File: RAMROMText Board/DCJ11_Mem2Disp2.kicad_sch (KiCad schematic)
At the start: 33 parts, among them J1 86093967113745ELF, U1 HM62256BLP, U2 SST39SF010, U3 GAL16V8, U4 74AHC138, U5 HM62256BLP, U6 SST39SF010

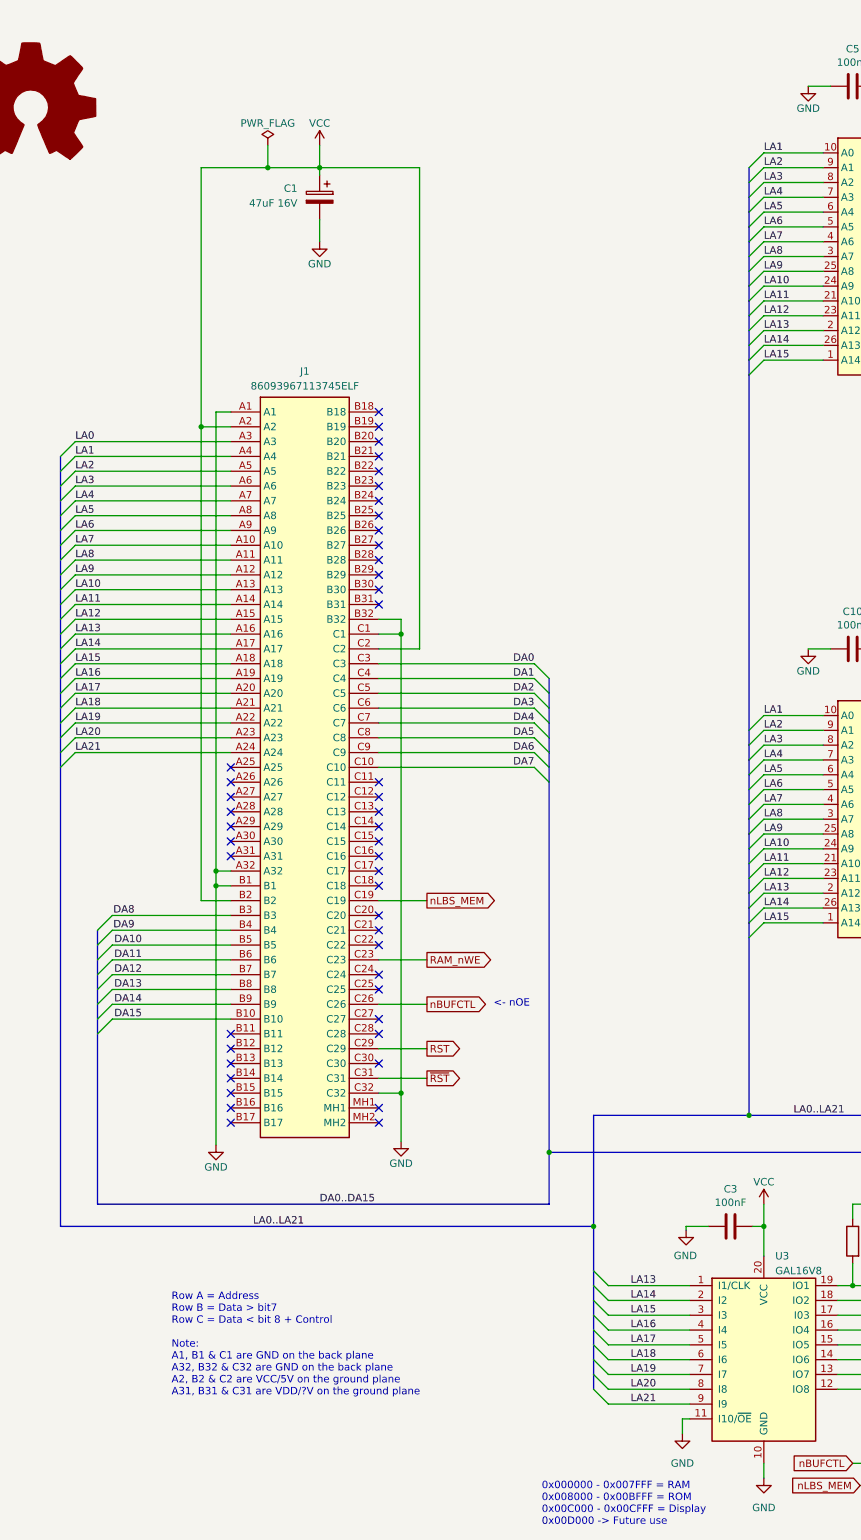
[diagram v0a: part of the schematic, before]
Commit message: Adjust memory map
Moved the memory map around so that I can add the dotmatrix display I want to add. These are now;

HEX
0x0000 - 0x7FFF = RAM  (32K)
0x6000 - 0x7FFF = Text Display (shadowed in RAM as it's WRITE only)
0x8000 - 0xBFFF = ROM  (16K)
0xC000 - 0xDFFF = Future (Matrix display)
0xE000 - 0xFFFF = Future

OCTAL (has to end on a multiple of 2)
000 000 - 077 776 - RAM
060 000 - 060 020 - Text Display (repeated multiple times)
100 000 - 137 776 - ROM
140 000 - 157 776 - Future (Matrix Display)
160 000 - 177 776 - Future
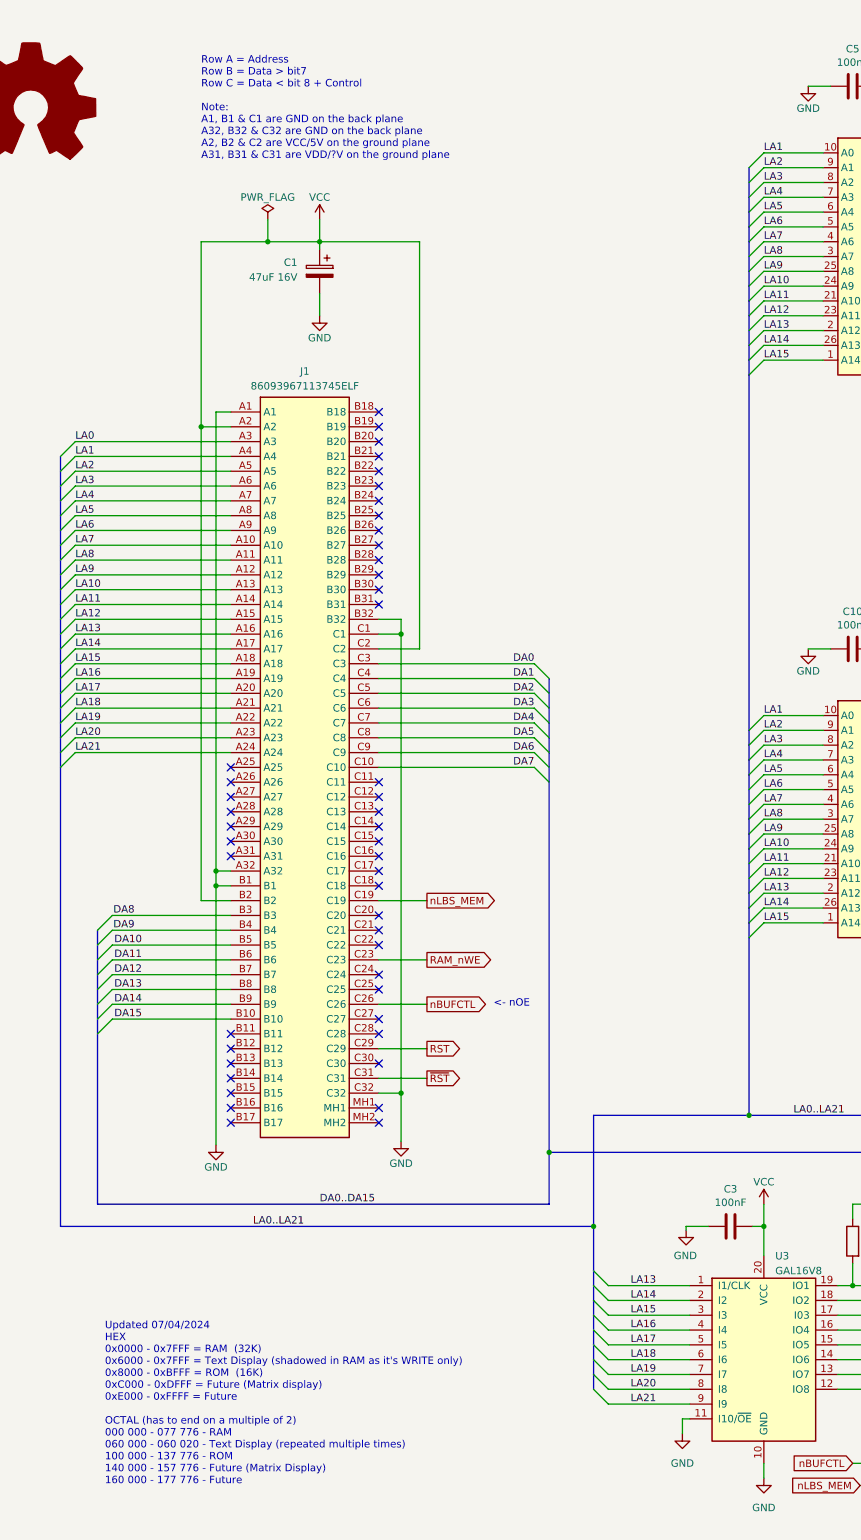
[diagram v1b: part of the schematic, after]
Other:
- note added: "Updated 07/04/2024 HEX 0x0000 - 0x7FFF = RAM (32K) 0x6000 - 0x7FFF = Text Display (shadowed in RAM as it's WRITE only) 0x8000 - 0xBFFF = ROM (16K) 0xC000 - 0xDFFF = Future (Matrix display) 0xE000 - 0xFFFF = Future OCTAL (has to end on a multiple of 2) 000 000 - 077 776 - RAM 060 000 - 060 020 - Text Display (repeated multiple times) 100 000 - 137 776 - ROM 140 000 - 157 776 - Future (Matrix Displ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"
- note removed: "0x000000 - 0x007FFF = RAM 0x008000 - 0x00BFFF = ROM 0x00C000 - 0x00CFFF = Display 0x00D000 -> Future use"
- moved on the sheet: C1
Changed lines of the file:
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@@
   (junction (at 347.98 105.41) (diameter 0) (color 0 0 0 0)
   )
-  (junction (at 81.28 45.72) (diameter 0) (color 0 0 0 0)
+  (junction (at 81.28 58.42) (diameter 0) (color 0 0 0 0)
   )
   (junction (at 154.94 208.28) (diameter 0) (color 0 0 0 0)
   )
-  (junction (at 72.39 45.72) (diameter 0) (color 0 0 0 0)
+  (junction (at 72.39 58.42) (diameter 0) (color 0 0 0 0)
   )
   (junction (at 336.55 48.26) (diameter 0) (color 0 0 0 0)
@@
     (stroke (width 0) (type default))
   )
-  (wire (pts (xy 98.425 45.72) (xy 98.425 128.27))
+  (wire (pts (xy 98.425 58.42) (xy 98.425 128.27))
     (stroke (width 0) (type default))
   )
@@
     (stroke (width 0) (type default))
   )
-  (wire (pts (xy 81.28 45.72) (xy 72.39 45.72))
+  (wire (pts (xy 81.28 58.42) (xy 72.39 58.42))
     (stroke (width 0) (type default))
   )
@@
     (stroke (width 0) (type default))
   )
-  (wire (pts (xy 72.39 45.72) (xy 72.39 41.91))
+  (wire (pts (xy 72.39 58.42) (xy 72.39 54.61))
     (stroke (width 0) (type default))
   )
@@
     (stroke (width 0) (type default))
   )
-  (wire (pts (xy 60.96 45.72) (xy 72.39 45.72))
+  (wire (pts (xy 60.96 58.42) (xy 72.39 58.42))
     (stroke (width 0) (type default))
   )
@@
     (stroke (width 0) (type default))
   )
-  (wire (pts (xy 81.28 45.72) (xy 81.28 41.91))
+  (wire (pts (xy 81.28 58.42) (xy 81.28 54.61))
     (stroke (width 0) (type default))
   )
@@
     (stroke (width 0) (type default))
   )
-  (wire (pts (xy 60.96 90.17) (xy 60.96 45.72))
+  (wire (pts (xy 60.96 90.17) (xy 60.96 58.42))
     (stroke (width 0) (type default))
   )
@@
     (stroke (width 0) (type default))
   )
-  (wire (pts (xy 81.28 54.61) (xy 81.28 58.42))
+  (wire (pts (xy 81.28 67.31) (xy 81.28 71.12))
     (stroke (width 0) (type default))
   )
@@
     (stroke (width 0) (type default))
   )
-  (wire (pts (xy 81.28 45.72) (xy 81.28 46.99))
+  (wire (pts (xy 81.28 58.42) (xy 81.28 59.69))
     (stroke (width 0) (type default))
   )
@@
     (stroke (width 0) (type default))
   )
-  (wire (pts (xy 81.28 45.72) (xy 98.425 45.72))
+  (wire (pts (xy 81.28 58.42) (xy 98.425 58.42))
     (stroke (width 0) (type default))
   )
@@
     (stroke (width 0) (type default))
   )
-  (text "0x000000 - 0x007FFF = RAM\n0x008000 - 0x00BFFF = ROM\n0x00C000 - 0x00CFFF = Display\n0x00D000 -> Future use\n"
-    (at 119.38 278.765 0)
+  (text "Updated 07/04/2024\nHEX\n0x0000 - 0x7FFF = RAM  (32K)\n0x6000 - 0x7FFF = Text Display (shadowed in RAM as it's WRITE only)\n0x8000 - 0xBFFF = ROM  (16K)\n0xC000 - 0xDFFF = Future (Matrix display)\n0xE000 - 0xFFFF = Future\n\nOCTAL (has to end on a multiple of 2)\n000 000 - 077 776 - RAM\n060 000 - 060 020 - Text Display (repeated multiple times)\n100 000 - 137 776 - ROM\n140 000 - 157 776 - Future (Matrix Display)\n160 000 - 177 776 - Future"
+    (at 44.45 271.78 0)
     (effects (font (size 1.27 1.27)) (justify left bottom))
   )
@@
   )
   (text "Row A = Address\nRow B = Data > bit7\nRow C = Data < bit 8 + Control\n\nNote:\nA1, B1 & C1 are GND on the back plane\nA32, B32 & C32 are GND on the back plane\nA2, B2 & C2 are VCC/5V on the ground plane\nA31, B31 & C31 are VDD/?V on the ground plane"
-    (at 55.88 256.54 0)
+    (at 60.96 44.45 0)
     (effects (font (size 1.27 1.27)) (justify left bottom))
   )
@@
     )
   )
-  (symbol (lib_id "power:PWR_FLAG") (at 72.39 41.91 0) (mirror y) (unit 1)
+  (symbol (lib_id "power:PWR_FLAG") (at 72.39 54.61 0) (mirror y) (unit 1)
     (in_bom yes) (on_board yes) (dnp no) (fields_autoplaced)
-    (property "Reference" "#FLG01" (at 72.39 40.005 0)
+    (property "Reference" "#FLG01" (at 72.39 52.705 0)
       (effects (font (size 1.27 1.27)) hide)
     )
-    (property "Value" "PWR_FLAG" (at 72.39 38.1 0)
+    (property "Value" "PWR_FLAG" (at 72.39 50.8 0)
       (effects (font (size 1.27 1.27)))
     )
-    (property "Footprint" "" (at 72.39 41.91 0)
+    (property "Footprint" "" (at 72.39 54.61 0)
       (effects (font (size 1.27 1.27)) hide)
     )
-    (property "Datasheet" "~" (at 72.39 41.91 0)
+    (property "Datasheet" "~" (at 72.39 54.61 0)
       (effects (font (size 1.27 1.27)) hide)
     )
@@
     )
   )
-  (symbol (lib_id "power:VCC") (at 81.28 41.91 0) (mirror y) (unit 1)
+  (symbol (lib_id "power:VCC") (at 81.28 54.61 0) (mirror y) (unit 1)
     (in_bom yes) (on_board yes) (dnp no) (fields_autoplaced)
-    (property "Reference" "#PWR02" (at 81.28 45.72 0)
+    (property "Reference" "#PWR02" (at 81.28 58.42 0)
       (effects (font (size 1.27 1.27)) hide)
     )
-    (property "Value" "VCC" (at 81.28 38.1 0)
+    (property "Value" "VCC" (at 81.28 50.8 0)
       (effects (font (size 1.27 1.27)))
     )
-    (property "Footprint" "" (at 81.28 41.91 0)
+    (property "Footprint" "" (at 81.28 54.61 0)
       (effects (font (size 1.27 1.27)) hide)
     )
-    (property "Datasheet" "" (at 81.28 41.91 0)
+    (property "Datasheet" "" (at 81.28 54.61 0)
       (effects (font (size 1.27 1.27)) hide)
     )
@@
     )
   )
-  (symbol (lib_id "power:GND") (at 81.28 58.42 0) (mirror y) (unit 1)
+  (symbol (lib_id "power:GND") (at 81.28 71.12 0) (mirror y) (unit 1)
     (in_bom yes) (on_board yes) (dnp no)
-    (property "Reference" "#PWR03" (at 81.28 64.77 0)
+    (property "Reference" "#PWR03" (at 81.28 77.47 0)
       (effects (font (size 1.27 1.27)) hide)
     )
-    (property "Value" "GND" (at 81.28 62.23 0)
+    (property "Value" "GND" (at 81.28 74.93 0)
       (effects (font (size 1.27 1.27)))
     )
-    (property "Footprint" "" (at 81.28 58.42 0)
+    (property "Footprint" "" (at 81.28 71.12 0)
       (effects (font (size 1.27 1.27)) hide)
     )
-    (property "Datasheet" "" (at 81.28 58.42 0)
+    (property "Datasheet" "" (at 81.28 71.12 0)
       (effects (font (size 1.27 1.27)) hide)
     )
@@
     )
   )
-  (symbol (lib_id "Device:C_Polarized") (at 81.28 50.8 0) (mirror y) (unit 1)
+  (symbol (lib_id "Device:C_Polarized") (at 81.28 63.5 0) (mirror y) (unit 1)
     (in_bom yes) (on_board yes) (dnp no) (fields_autoplaced)
-    (property "Reference" "C1" (at 77.47 49.276 0)
+    (property "Reference" "C1" (at 77.47 61.976 0)
       (effects (font (size 1.27 1.27)) (justify left))
     )
-    (property "Value" "47uF 16V" (at 77.47 51.816 0)
+    (property "Value" "47uF 16V" (at 77.47 64.516 0)
       (effects (font (size 1.27 1.27)) (justify left))
     )
-    (property "Footprint" "Capacitor_SMD:CP_Elec_6.3x5.8" (at 80.3148 54.61 0)
+    (property "Footprint" "Capacitor_SMD:CP_Elec_6.3x5.8" (at 80.3148 67.31 0)
       (effects (font (size 1.27 1.27)) hide)
     )
-    (property "Datasheet" "~" (at 81.28 50.8 0)
+    (property "Datasheet" "~" (at 81.28 63.5 0)
       (effects (font (size 1.27 1.27)) hide)
     )
